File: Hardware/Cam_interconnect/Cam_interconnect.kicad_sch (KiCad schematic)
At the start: 6 parts, among them J1 Conn_02x06_Odd_Even, J2 Conn_01x06, U1 SN65LVDT14PW

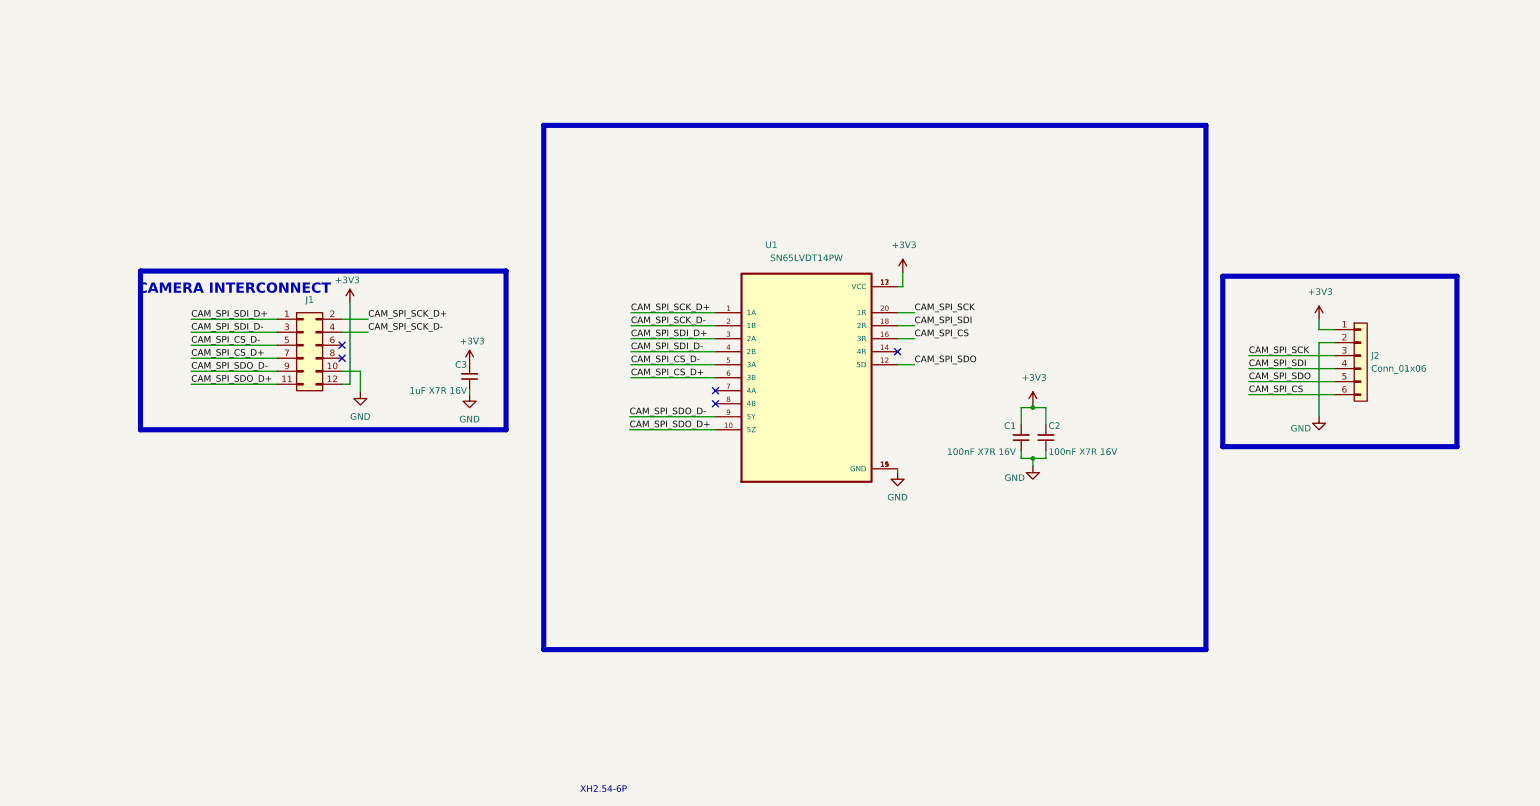
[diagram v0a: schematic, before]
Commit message: Updated the pdf for main board schematics
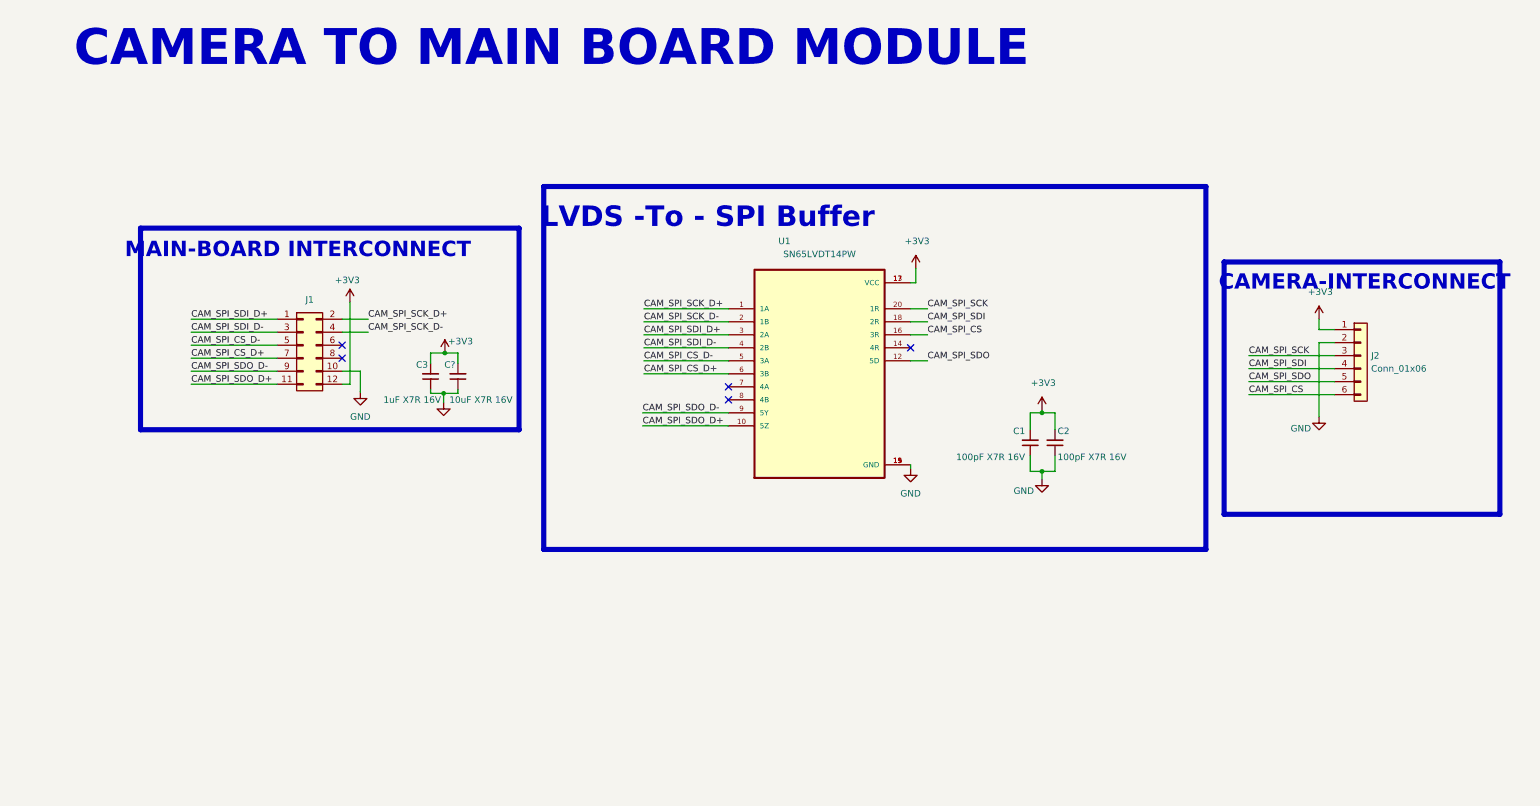
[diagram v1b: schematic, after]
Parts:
- added C?: 10uF X7R 16V, Capacitor_SMD:C_0402_1005Metric, symbol Device:C_Small
- C1, C2: value 100nF X7R 16V -> 100pF X7R 16V
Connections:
- net +3V3: now also C?.2
- net GND: now also C?.1
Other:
- note added: "CAMERA TO MAIN BOARD MODULE"
- note added: "CAMERA-INTERCONNECT"
- note added: "LVDS -To - SPI Buffer"
- note added: "MAIN-BOARD INTERCONNECT"
- note removed: "CAMERA INTERCONNECT"
- note removed: "XH2.54-6P"
- company: (none) -> HGO
- title: (none) -> TraxXTure - Cam-Board
- moved on the sheet: C1, C2, C3, U1
